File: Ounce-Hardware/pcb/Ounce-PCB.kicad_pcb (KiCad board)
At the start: 2 copper layers, 135 x 61 mm, 5 parts, among them U1 RaspberryPi_Pico2_W, U2 RaspberryPi_Pico, U3 RaspberryPi_Pico, U4 RaspberryPi_Pico, U5 RaspberryPi_Pico

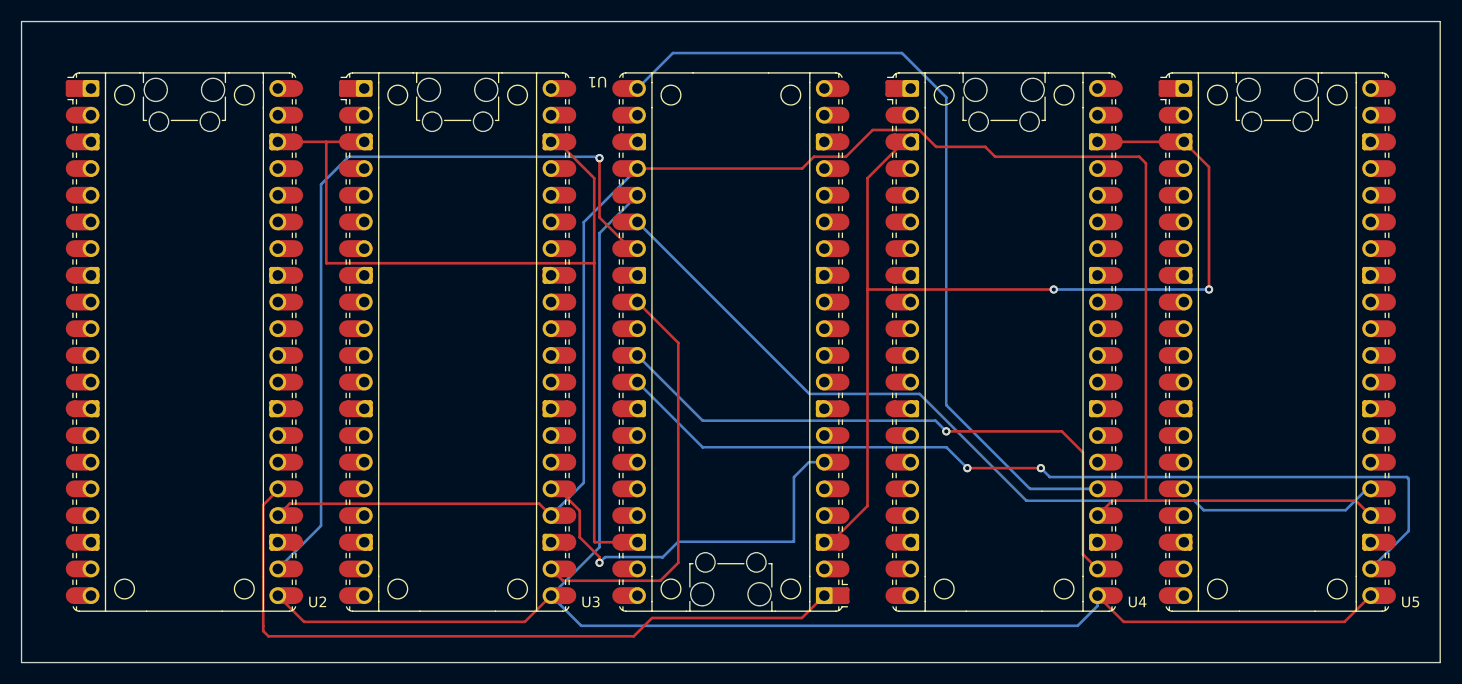
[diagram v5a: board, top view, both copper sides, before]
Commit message: Route MOSI and SCK per slave, drop a dangling MOSI stub
MOSI and SCK now branch to each slave rather than running as one chain, and the
leftover 3.53mm MOSI stub at (106.890, 124.130) is gone - one end connected to
nothing, left over from the reroute.

Checked before removing that every MOSI pad stays on the same network without
it, and it does: five pads, one network, and track_dangling is clear.

Also correcting the earlier reading of the ground. Counting copper networks was
the wrong test. No slave is load-bearing - U3 and U4 each have both ground pads
in one network and U2 and U5 are leaves - so every remaining slave keeps a
copper path to the master with any one or two slaves removed, which is what the
wiring needed to do. The two networks meet at U1 pins 3 and 38, the same node
inside the master, and the master has to be present for the bus to exist at all.

Co-Authored-By: Claude Opus 5 <noreply@anthropic.com>
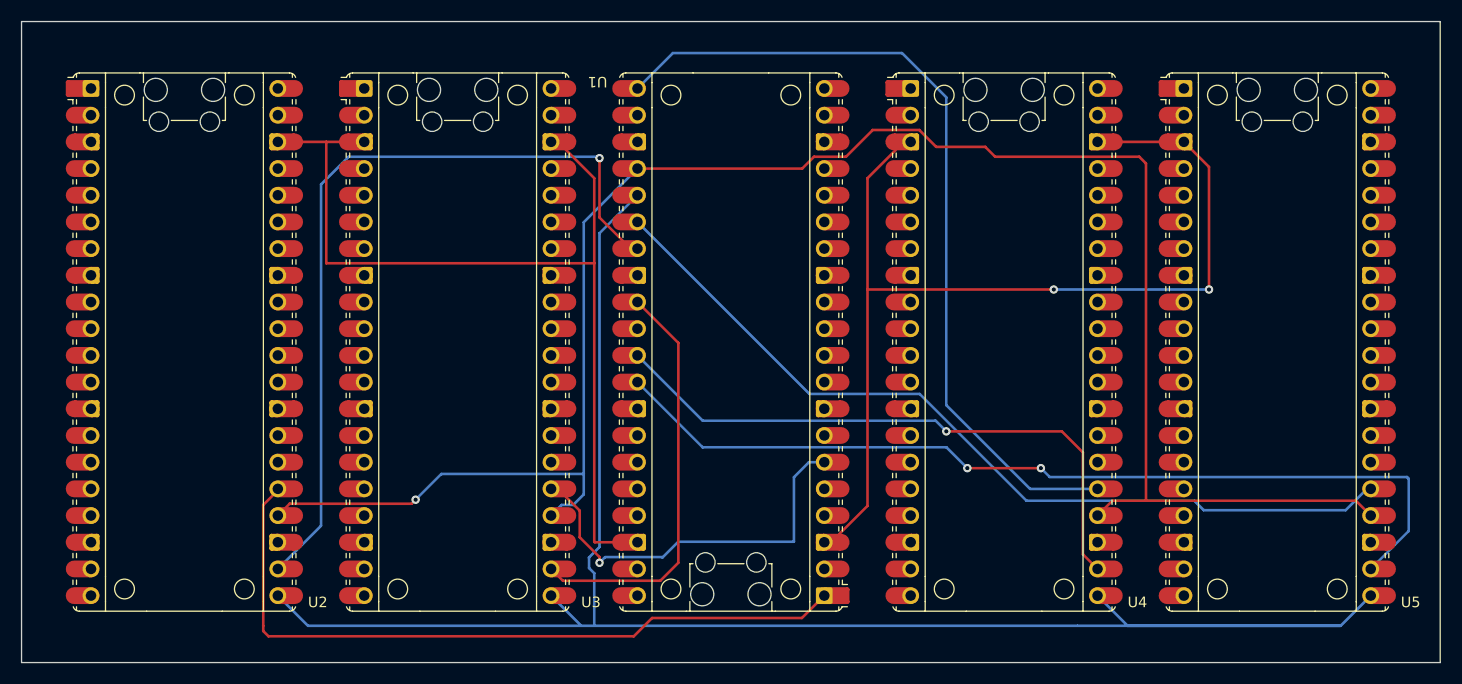
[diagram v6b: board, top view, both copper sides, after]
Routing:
- net SPI0_MOSI: track 152.6 -> 177.8 mm
- net SPI0_SCK: track 173.9 -> 178.3 mm, vias 0 -> 1
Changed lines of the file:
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@@
 	)
 	(segment
-		(start 109.385 126.625)
-		(end 130.395 126.625)
-		(width 0.25)
-		(layer "F.Cu")
-		(net "SPI0_MOSI")
-	)
-	(segment
-		(start 130.395 126.625)
-		(end 132.89 124.13)
-		(width 0.25)
-		(layer "F.Cu")
+		(start 141.11 86.03)
+		(end 137.5 89.64)
+		(width 0.25)
+		(layer "B.Cu")
+		(net "SPI0_MOSI")
+	)
+	(segment
+		(start 183 127)
+		(end 137 127)
+		(width 0.25)
+		(layer "B.Cu")
+		(net "SPI0_MOSI")
+	)
+	(segment
+		(start 137.5 119.5)
+		(end 136.5 120.5)
+		(width 0.25)
+		(layer "B.Cu")
+		(net "SPI0_MOSI")
+	)
+	(segment
+		(start 187.76 127)
+		(end 184.89 124.13)
+		(width 0.25)
+		(layer "B.Cu")
+		(net "SPI0_MOSI")
+	)
+	(segment
+		(start 135.76 127)
+		(end 109.76 127)
+		(width 0.25)
+		(layer "B.Cu")
 		(net "SPI0_MOSI")
 	)
 	(segment
 		(start 210.89 124.13)
-		(end 208.395 126.625)
-		(width 0.25)
-		(layer "F.Cu")
-		(net "SPI0_MOSI")
-	)
-	(segment
-		(start 208.395 126.625)
-		(end 187.385 126.625)
-		(width 0.25)
-		(layer "F.Cu")
-		(net "SPI0_MOSI")
-	)
-	(segment
-		(start 187.385 126.625)
-		(end 184.89 124.13)
-		(width 0.25)
-		(layer "F.Cu")
-		(net "SPI0_MOSI")
-	)
-	(segment
-		(start 106.89 124.13)
-		(end 109.385 126.625)
-		(width 0.25)
-		(layer "F.Cu")
-		(net "SPI0_MOSI")
-	)
-	(segment
-		(start 183 127)
-		(end 135.76 127)
-		(width 0.25)
-		(layer "B.Cu")
-		(net "SPI0_MOSI")
-	)
-	(segment
-		(start 132.89 124.13)
-		(end 137.5 119.52)
-		(width 0.25)
-		(layer "B.Cu")
-		(net "SPI0_MOSI")
-	)
-	(segment
-		(start 137.5 119.52)
-		(end 137.5 89.64)
+		(end 208.02 127)
+		(width 0.25)
+		(layer "B.Cu")
+		(net "SPI0_MOSI")
+	)
+	(segment
+		(start 137.5 89.64)
+		(end 137.5 119.5)
+		(width 0.25)
+		(layer "B.Cu")
+		(net "SPI0_MOSI")
+	)
+	(segment
+		(start 137 122)
+		(end 137 127)
+		(width 0.25)
+		(layer "B.Cu")
+		(net "SPI0_MOSI")
+	)
+	(segment
+		(start 136.5 120.5)
+		(end 136.5 121.5)
+		(width 0.25)
+		(layer "B.Cu")
+		(net "SPI0_MOSI")
+	)
+	(segment
+		(start 136.5 121.5)
+		(end 137 122)
+		(width 0.25)
+		(layer "B.Cu")
+		(net "SPI0_MOSI")
+	)
+	(segment
+		(start 208.02 127)
+		(end 183 127)
 		(width 0.25)
 		(layer "B.Cu")
@@
 	)
 	(segment
-		(start 137.5 89.64)
-		(end 141.11 86.03)
-		(width 0.25)
-		(layer "B.Cu")
-		(net "SPI0_MOSI")
-	)
-	(segment
-		(start 184.89 124.13)
-		(end 184.89 125.11)
-		(width 0.25)
-		(layer "B.Cu")
-		(net "SPI0_MOSI")
-	)
-	(segment
-		(start 184.89 125.11)
-		(end 183 127)
+		(start 109.76 127)
+		(end 106.89 124.13)
+		(width 0.25)
+		(layer "B.Cu")
+		(net "SPI0_MOSI")
+	)
+	(segment
+		(start 208.02 127)
+		(end 187.76 127)
+		(width 0.25)
+		(layer "B.Cu")
+		(net "SPI0_MOSI")
+	)
+	(segment
+		(start 137 127)
+		(end 135.76 127)
 		(width 0.25)
 		(layer "B.Cu")
@@
 	)
 	(segment
-		(start 132.89 116.51)
-		(end 131.765 115.385)
+		(start 108.015 115.385)
+		(end 106.89 116.51)
 		(width 0.25)
 		(layer "F.Cu")
@@
 	)
 	(segment
+		(start 119.615 115.385)
+		(end 108.015 115.385)
+		(width 0.25)
+		(layer "F.Cu")
+		(net "SPI0_SCK")
+	)
+	(segment
 		(start 184.89 116.51)
 		(end 186.305 115.095)
@@
 	)
 	(segment
-		(start 108.015 115.385)
-		(end 106.89 116.51)
-		(width 0.25)
-		(layer "F.Cu")
-		(net "SPI0_SCK")
-	)
-	(segment
-		(start 131.765 115.385)
-		(end 108.015 115.385)
-		(width 0.25)
-		(layer "F.Cu")
-		(net "SPI0_SCK")
-	)
-	(segment
 		(start 174.20586 81.425)
 		(end 169.534534 81.425)
@@
 	)
 	(segment
-		(start 136 113.4)
-		(end 132.89 116.51)
+		(start 120 115)
+		(end 119.615 115.385)
+		(width 0.25)
+		(layer "F.Cu")
+		(net "SPI0_SCK")
+	)
+	(via
+		(at 120 115)
+		(size 0.8)
+		(drill 0.4)
+		(layers "F.Cu" "B.Cu")
+		(net "SPI0_SCK")
+	)
+	(segment
+		(start 122.445 112.555)
+		(end 120 115)
+		(width 0.25)
+		(layer "B.Cu")
+		(net "SPI0_SCK")
+	)
+	(segment
+		(start 136 114.5)
+		(end 135 115.5)
+		(width 0.25)
+		(layer "B.Cu")
+		(net "SPI0_SCK")
+	)
+	(segment
+		(start 136 112.5)
+		(end 135.945 112.555)
+		(width 0.25)
+		(layer "B.Cu")
+		(net "SPI0_SCK")
+	)
+	(segment
+		(start 135 115.5)
+		(end 133.9 115.5)
+		(width 0.25)
+		(layer "B.Cu")
+		(net "SPI0_SCK")
+	)
+	(segment
+		(start 135.945 112.555)
+		(end 122.445 112.555)
 		(width 0.25)
 		(layer "B.Cu")
@@
 	)
 	(segment
+		(start 133.9 115.5)
+		(end 132.89 116.51)
+		(width 0.25)
+		(layer "B.Cu")
+		(net "SPI0_SCK")
+	)
+	(segment
 		(start 136 88.6)
-		(end 136 113.4)
-		(width 0.25)
-		(layer "B.Cu")
+		(end 136 112.5)
+		(width 0.25)
+		(layer "B.Cu")
+		(net "SPI0_SCK")
+	)
+	(segment
+		(start 136 112.5)
+		(end 136 114.5)
+		(width 0.25)
+		(layer "B.Cu")

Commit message: Turn the silkscreen to read from the master's USB end
The back text was upright when the board is held with the servants' USB ports
up. The master is rotated 180 so its USB faces the other way, and the text now
reads from that end instead: the whole block rotated 180 about the board centre
at (150,100), each text's own angle turned with it.

The rows still fit because the clear band they were fitted into, y 81..119, is
symmetric about y=100, so the block maps onto itself. No silkscreen violations.

Also removed six sub-0.2mm track slivers left by interactive routing, the
largest 0.19mm and the smallest 0.03mm, on MOSI, CS0, SCK, MISO0 and MISO1.
DRC reports the same three unconnected ground pads before and after, so nothing
depended on them, and track_dangling is now clear.

Ground robustness re-checked against the current routing: no slave is
load-bearing, and every remaining slave keeps a copper path to the master with
any one or two removed.

Co-Authored-By: Claude Opus 5 <noreply@anthropic.com>
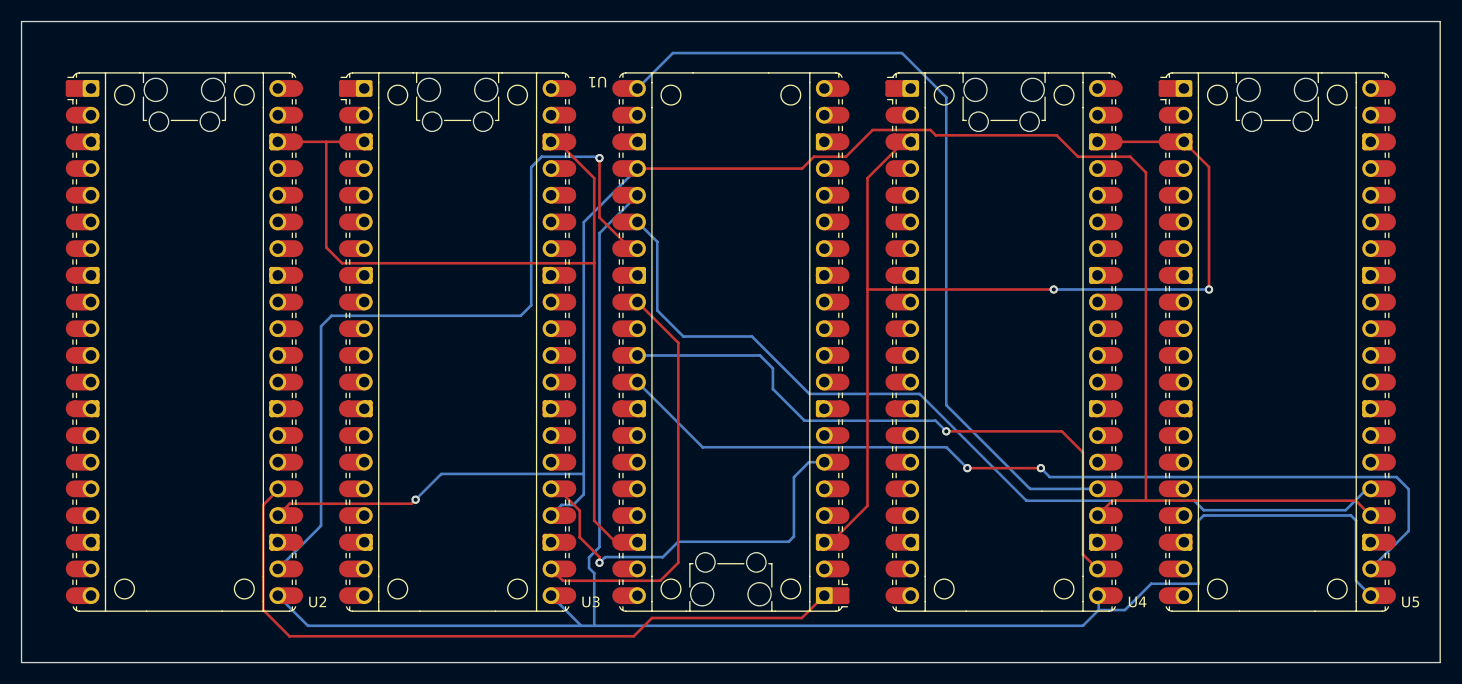
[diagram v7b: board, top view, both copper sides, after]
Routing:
- net SPI0_MOSI: track 177.8 -> 168.0 mm
- net SPI0_MISO3: track 82.0 -> 85.8 mm
- net GND: track 187.6 -> 185.5 mm
- net SPI0_MISO0: track 69.3 -> 68.0 mm
- net SPI0_CS2: track 57.9 -> 59.0 mm
- net SPI0_CS3: track 87.3 -> 86.7 mm
- net SPI0_SCK: track 178.3 -> 177.8 mm

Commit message: Clear three more routing slivers
Interactive routing left three more sub-0.2mm fragments: CS3 at 0.015mm and
0.021mm, MISO3 at 0.040mm. DRC flagged none of them - they are too short to
register as dangling - so they would have gone to fab unnoticed.

Each was tested on its own this time before removing anything, and then all
three together: unconnected stays at 3 in every case, so nothing depended on
them. Board is now 147 segments, 8 vias, 1062mm of copper, no fragments left.

Co-Authored-By: Claude Opus 5 <noreply@anthropic.com>
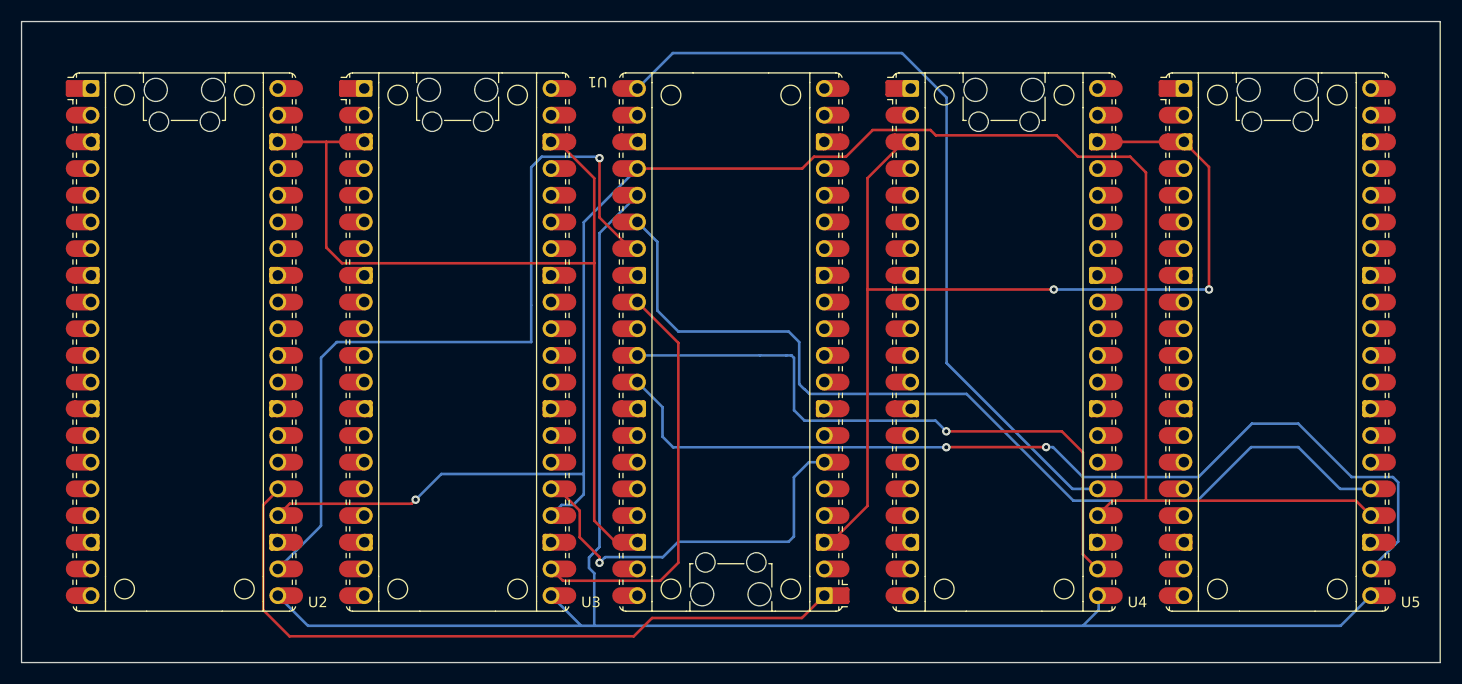
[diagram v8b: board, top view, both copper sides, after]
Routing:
- net SPI0_MOSI: track 168.0 -> 156.9 mm
- net SPI0_MISO3: track 85.8 -> 90.7 mm
- net SPI0_CS3: track 86.7 -> 91.5 mm
- net SPI0_MISO2: track 79.5 -> 77.1 mm
- net SPI0_CS2: track 59.0 -> 60.8 mm
